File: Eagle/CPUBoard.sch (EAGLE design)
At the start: 32 parts, among them IC2 MAX232, IC3 MAX485CPA, Q1 12.000MHz, X2 RELAY_BOARD, X3 RS-485, X4 DISPLAY, X5 RS-232, X6 MKDSN1,5/3-5,08, X7 MKDSN1,5/3-5,08, X8 BUTTON_BOARD

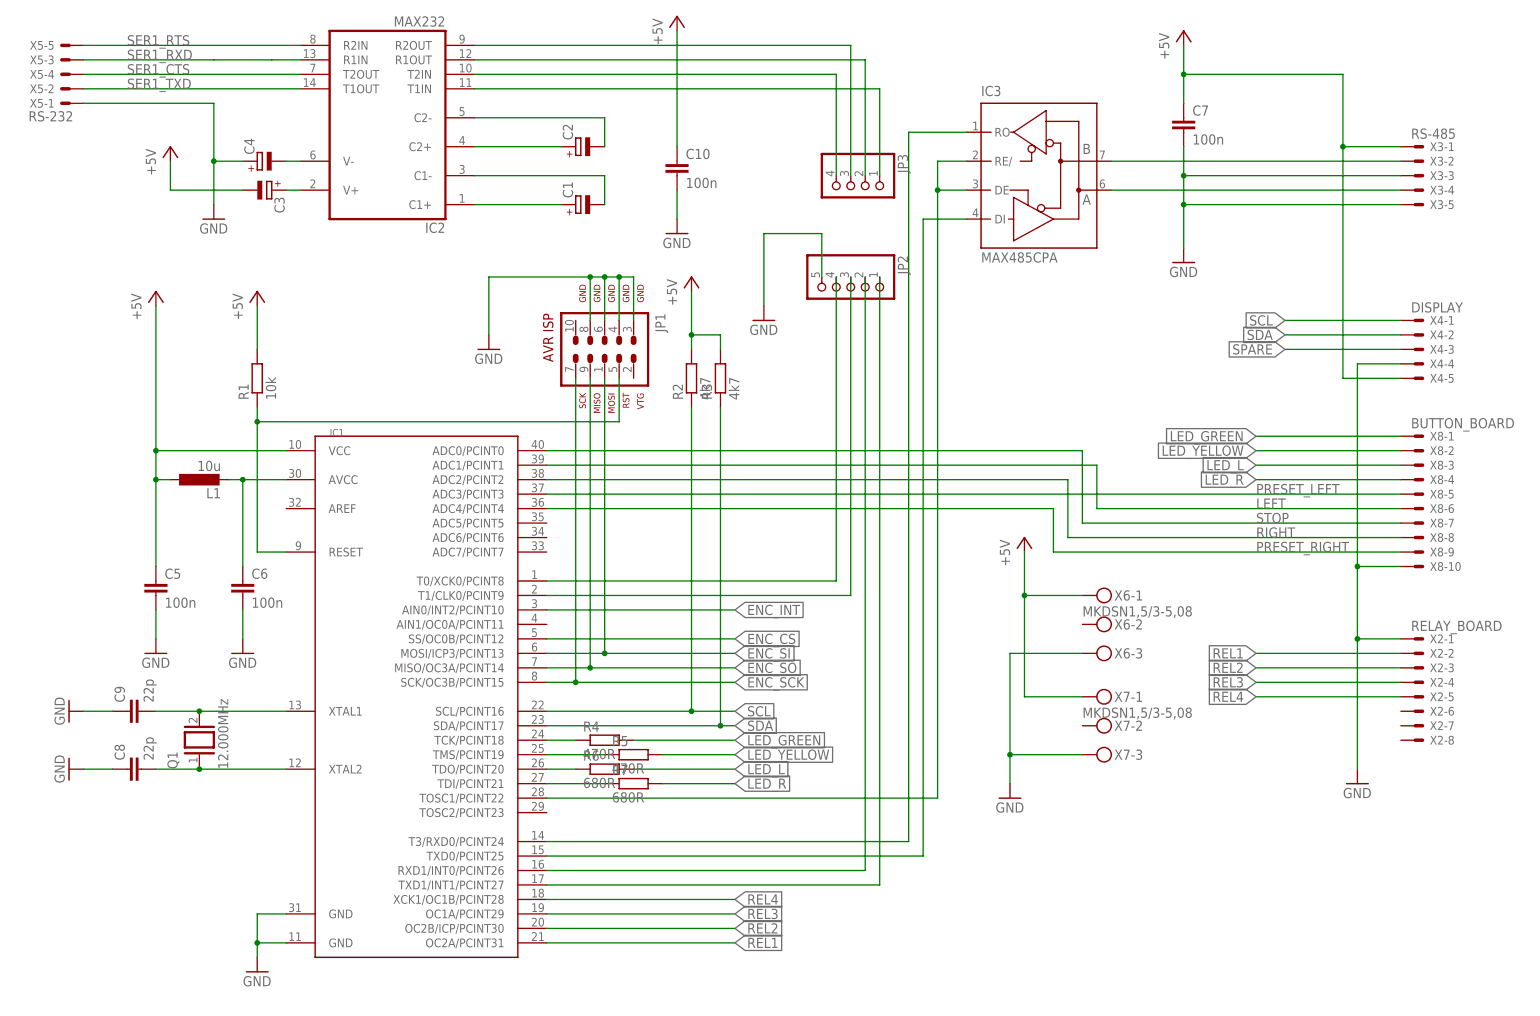
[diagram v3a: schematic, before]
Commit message: - CPUBoard with some corrections - two-sided board routed (demo), component placement
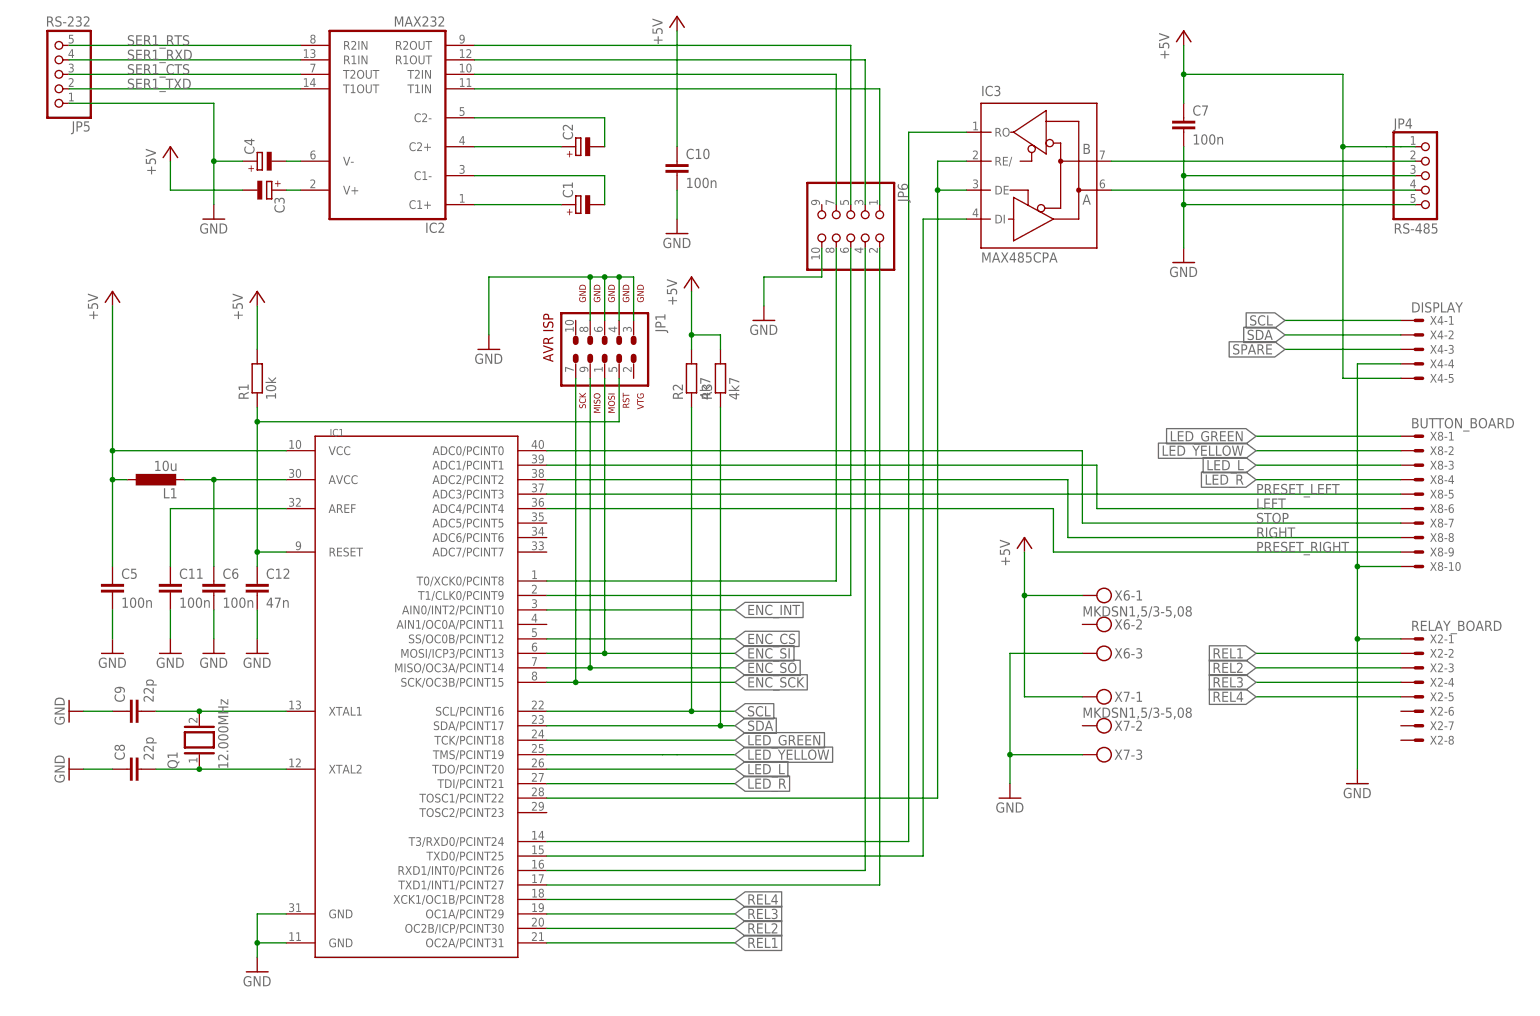
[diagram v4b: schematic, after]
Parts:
- removed JP2: (no value), pinhead:PINHD-1X5
- removed JP3: (no value), pinhead:PINHD-1X4
- removed R4, R5: 470R, rcl:R-EU_0207/10
- removed R6, R7: 680R, rcl:R-EU_0207/10
- removed X3: RS-485, con-molex:KK-156-5
- removed X5: RS-232, con-molex:KK-156-5
- added C11: 100n, rcl:C-EU025-025X050
- added C12: 47n, rcl:C-EU025-025X050
- added JP4: RS-485, pinhead:PINHD-1X5
- added JP5: RS-232, pinhead:PINHD-1X5
- added JP6: (no value), pinhead:PINHD-2X5
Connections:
- removed net N$20: IC1.TCK/PCINT18, R4.1
- removed net N$21: IC1.TMS/PCINT19, R5.1
- removed net N$22: IC1.TDO/PCINT20, R6.1
- removed net N$23: IC1.TDI/PCINT21, R7.1
- new net N$19: C11.1, IC1.AREF
- net +5V: now also JP4.1; no longer X3-1.S
- net GND: now also C11.2, C12.2, JP4.3, JP4.5, JP5.1, JP6.10; no longer JP2.5, X3-3.S, X3-5.S, X5-1.S
- net LED_GREEN: now also IC1.TCK/PCINT18; no longer R4.2
- net LED_L: now also IC1.TDO/PCINT20; no longer R6.2
- net LED_R: now also IC1.TDI/PCINT21; no longer R7.2
- net LED_YELLOW: now also IC1.TMS/PCINT19; no longer R5.2
- net N$11: now also JP6.3; no longer JP3.2
- net N$16: now also JP6.4; no longer JP2.2
- net N$17: now also JP4.4; no longer X3-4.S
- net N$18: now also JP4.2; no longer X3-2.S
- net N$24: now also JP6.2; no longer JP2.1
- net N$28: now also JP6.5; no longer JP3.3
- net N$29: now also JP6.7; no longer JP3.4
- net N$3: now also C12.1
- net N$30: now also JP6.6; no longer JP2.3
- net N$31: now also JP6.8; no longer JP2.4
- net N$4: now also JP6.1; no longer JP3.1
- net SER1_CTS: now also JP5.3; no longer X5-4.S
- net SER1_RTS: now also JP5.5; no longer X5-5.S
- net SER1_RXD: now also JP5.4; no longer X5-3.S
- net SER1_TXD: now also JP5.2; no longer X5-2.S
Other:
- moved on the sheet: C5, C6, L1

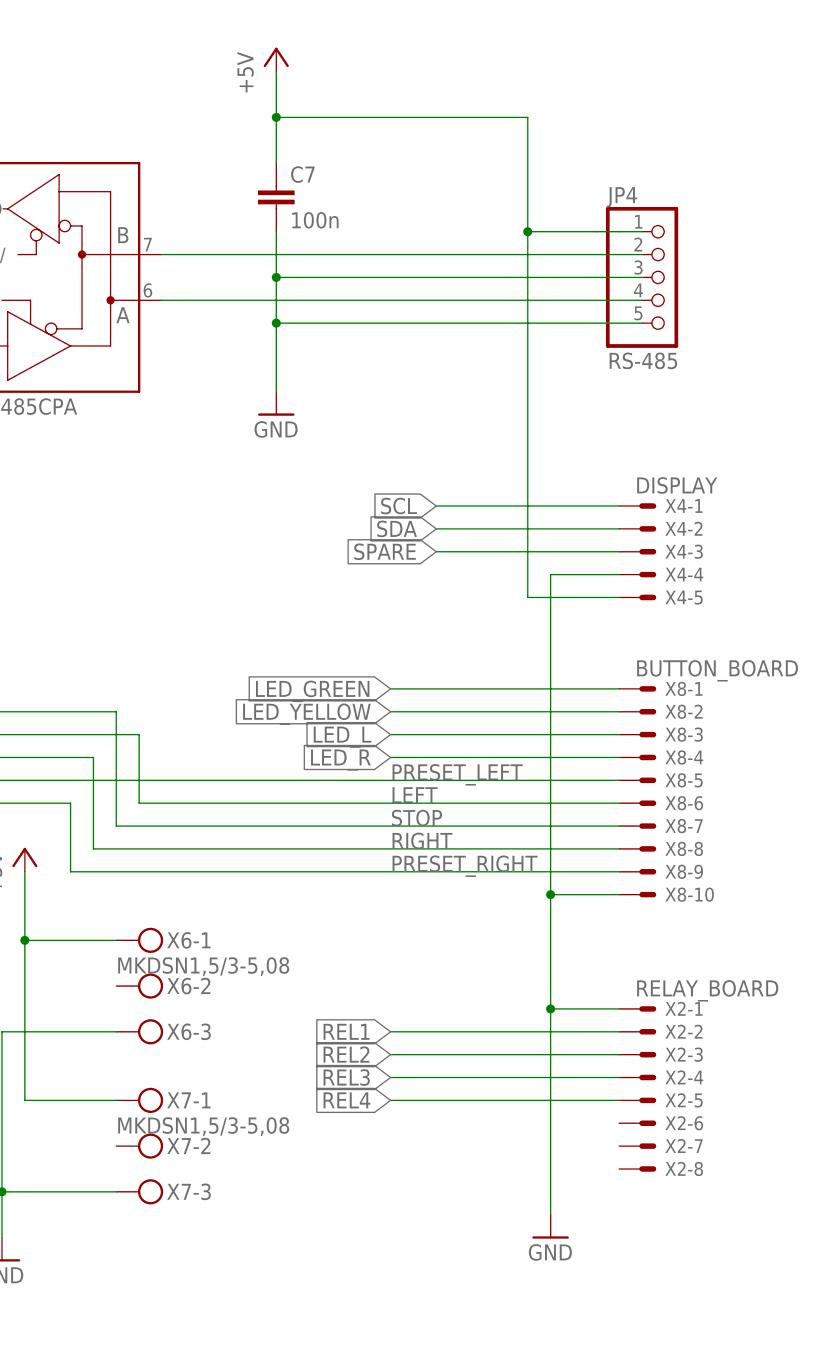
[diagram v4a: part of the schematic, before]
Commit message: - corrections for CPUBoard:   - RS-485 need termination resistors etc.   - connectors are wrong, use 22-?-05 tec. from con-molex -> connectors on other boards must be replaced, too!
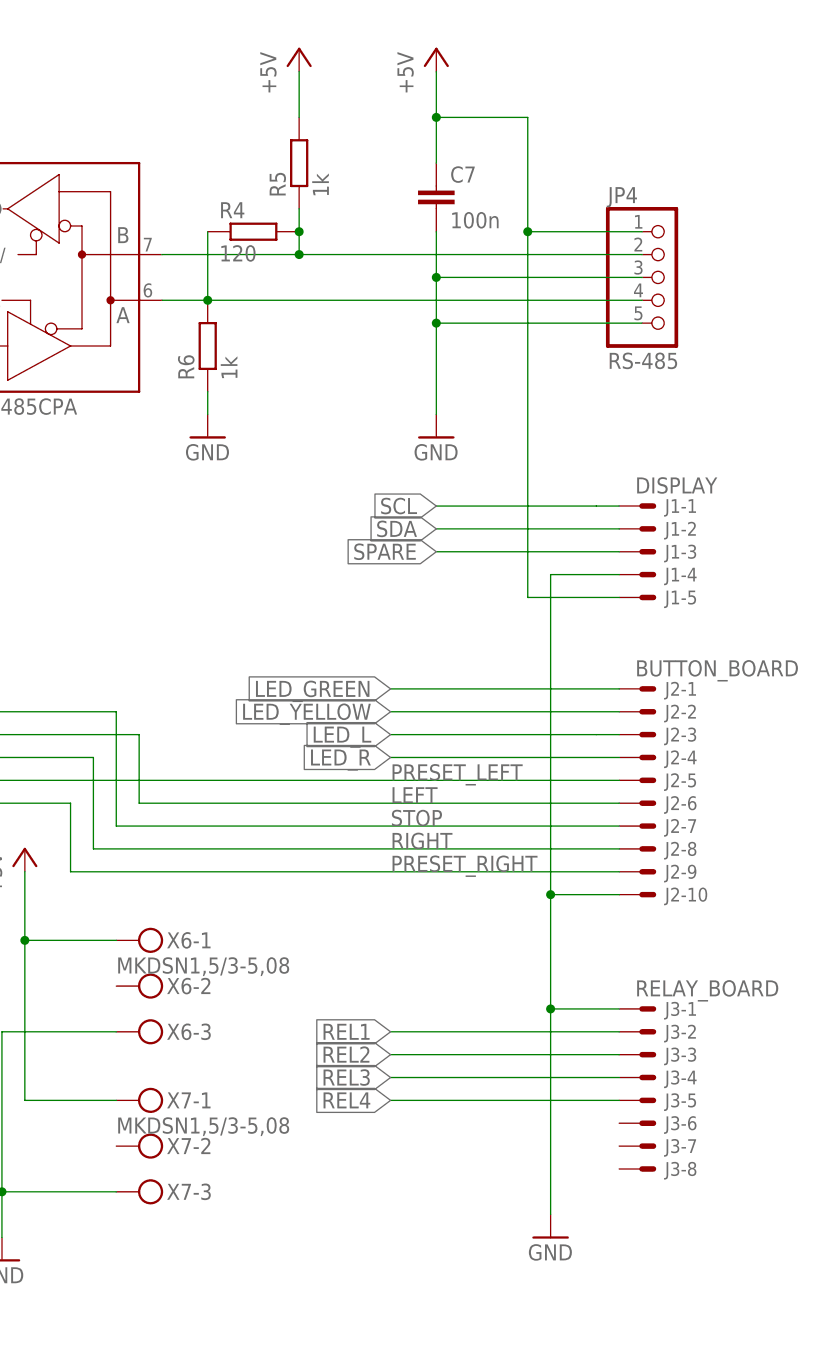
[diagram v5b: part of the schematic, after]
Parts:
- removed X2: RELAY_BOARD, con-molex:KK-156-8
- removed X4: DISPLAY, con-molex:KK-156-5
- removed X8: BUTTON_BOARD, con-molex:KK-156-10
- added J1: DISPLAY, con-molex:22-27-2051-05
- added J2: BUTTON_BOARD, con-molex:22-27-2101-10
- added J3: RELAY_BOARD, con-molex:22-27-2081-08
- added R4: 120, rcl:R-EU_0207/10
- added R5, R6: 1k, rcl:R-EU_0207/10
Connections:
- net +5V: now also J1-5.S, R5.2; no longer X4-5.S
- net GND: now also J1-4.S, J2-10.S, J3-1.S, R6.1; no longer X2-1.S, X4-4.S, X8-10.S
- net LED_GREEN: now also J2-1.S; no longer X8-1.S
- net LED_L: now also J2-3.S; no longer X8-3.S
- net LED_R: now also J2-4.S; no longer X8-4.S
- net LED_YELLOW: now also J2-2.S; no longer X8-2.S
- net LEFT: now also J2-6.S; no longer X8-6.S
- net N$17: now also R4.1, R6.2
- net N$18: now also R4.2, R5.1
- net PRESET_LEFT: now also J2-5.S; no longer X8-5.S
- net PRESET_RIGHT: now also J2-9.S; no longer X8-9.S
- net REL1: now also J3-2.S; no longer X2-2.S
- net REL2: now also J3-3.S; no longer X2-3.S
- net REL3: now also J3-4.S; no longer X2-4.S
- net REL4: now also J3-5.S; no longer X2-5.S
- net RIGHT: now also J2-8.S; no longer X8-8.S
- net SCL: now also J1-1.S; no longer X4-1.S
- net SDA: now also J1-2.S; no longer X4-2.S
- net SPARE: now also J1-3.S; no longer X4-3.S
- net STOP: now also J2-7.S; no longer X8-7.S
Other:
- moved on the sheet: C7
